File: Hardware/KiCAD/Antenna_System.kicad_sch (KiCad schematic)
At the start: 21 parts, among them IC4 SA630D_01,118, IC6 SA630D_01,118, J2 Conn_Coaxial_UHF

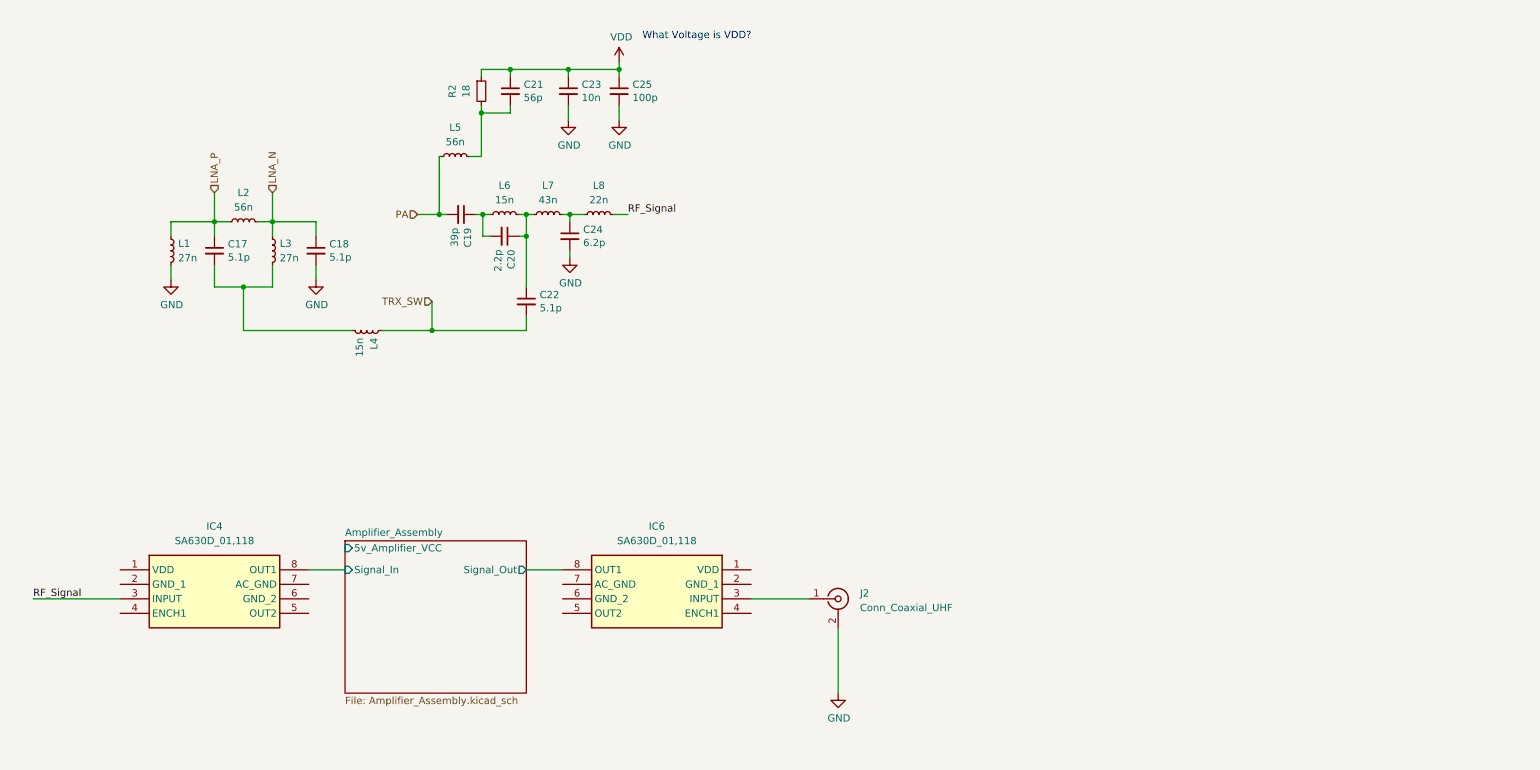
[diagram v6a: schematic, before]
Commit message: feat: subsystem exploration, begin placement, routing #11 #12 #4 many new project symbols
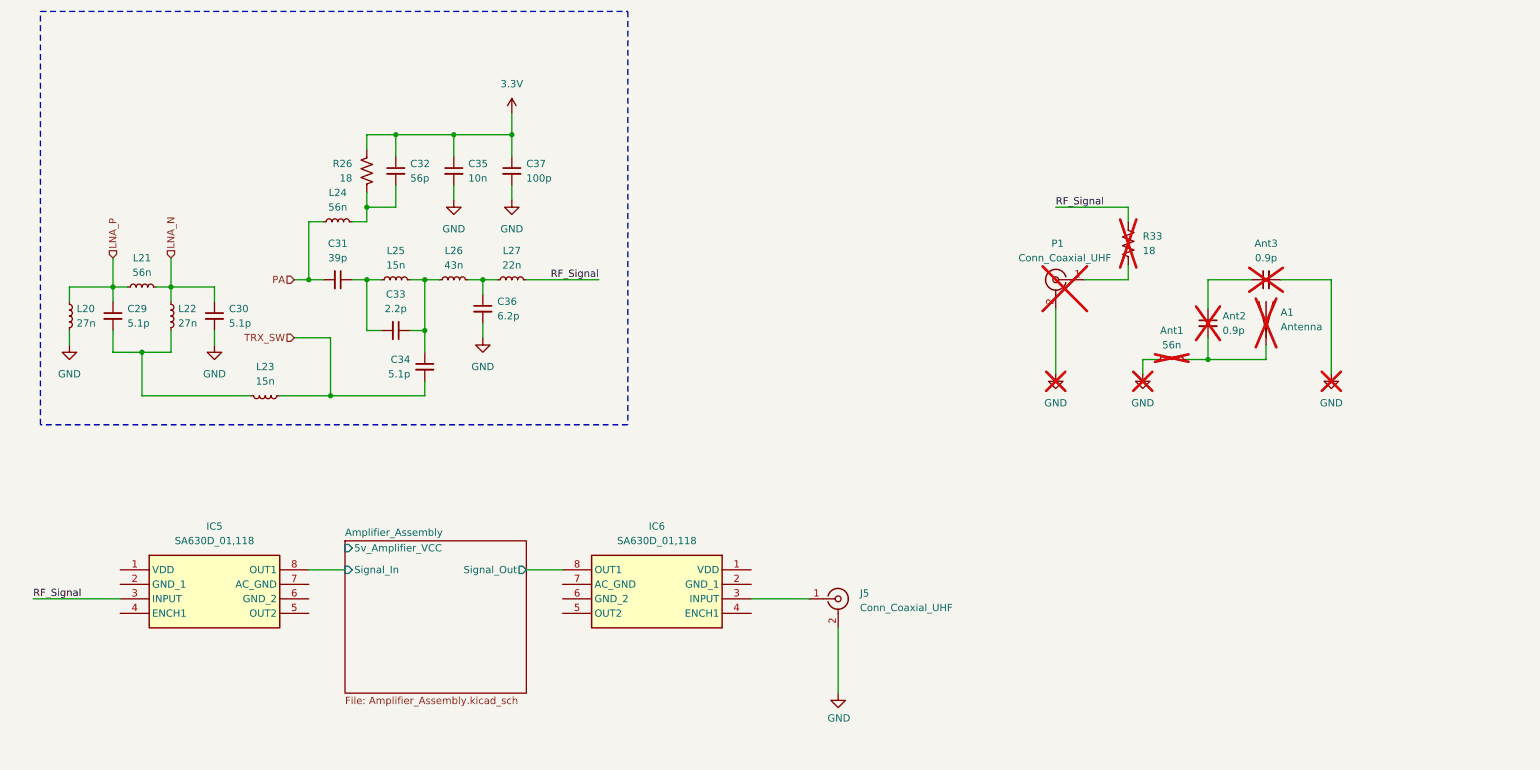
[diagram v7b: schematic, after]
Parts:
- removed C17, C18, C22: 5.1p, Capacitor_SMD:C_0402_1005Metric, symbol pkl_device:pkl_C_Small
- removed C19: 39p, Capacitor_SMD:C_0402_1005Metric, symbol pkl_device:pkl_C_Small
- removed C20: 2.2p, Capacitor_SMD:C_0402_1005Metric, symbol pkl_device:pkl_C_Small
- removed C21: 56p, Capacitor_SMD:C_0402_1005Metric, symbol pkl_device:pkl_C_Small
- removed C23: 10n, Capacitor_SMD:C_0402_1005Metric, symbol pkl_device:pkl_C_Small
- removed C24: 6.2p, Capacitor_SMD:C_0402_1005Metric, symbol pkl_device:pkl_C_Small
- removed C25: 100p, Capacitor_SMD:C_0402_1005Metric, symbol pkl_device:pkl_C_Small
- removed L1, L3: 27n, Inductor_SMD:L_0402_1005Metric, symbol Device:L_Small
- removed L2, L5: 56n, Inductor_SMD:L_0402_1005Metric, symbol Device:L_Small
- removed L4, L6: 15n, Inductor_SMD:L_0402_1005Metric, symbol Device:L_Small
- removed L7: 43n, Inductor_SMD:L_0402_1005Metric, symbol Device:L_Small
- removed L8: 22n, Inductor_SMD:L_0402_1005Metric, symbol Device:L_Small
- removed R2: 18, Resistor_SMD:R_0402_1005Metric, symbol pkl_device:pkl_R_Small
- added A1: Antenna, symbol Device:Antenna
- added Ant1, L21, L24: 56n, Inductor_SMD:L_0402_1005Metric, symbol Device:L_Small
- added Ant2, Ant3: 0.9p, Capacitor_SMD:C_0402_1005Metric, symbol Device:C_Small
- added C29, C30, C34: 5.1p, Capacitor_SMD:C_0402_1005Metric, symbol Device:C_Small
- added C31: 39p, Capacitor_SMD:C_0402_1005Metric, symbol Device:C_Small
- added C32: 56p, Capacitor_SMD:C_0402_1005Metric, symbol Device:C_Small
- added C33: 2.2p, Capacitor_SMD:C_0402_1005Metric, symbol Device:C_Small
- added C35: 10n, Capacitor_SMD:C_0402_1005Metric, symbol Device:C_Small
- added C36: 6.2p, Capacitor_SMD:C_0402_1005Metric, symbol Device:C_Small
- added C37: 100p, Capacitor_SMD:C_0402_1005Metric, symbol Device:C_Small
- added L20, L22: 27n, Inductor_SMD:L_0402_1005Metric, symbol Device:L_Small
- added L23, L25: 15n, Inductor_SMD:L_0402_1005Metric, symbol Device:L_Small
- added L26: 43n, Inductor_SMD:L_0402_1005Metric, symbol Device:L_Small
- added L27: 22n, Inductor_SMD:L_0402_1005Metric, symbol Device:L_Small
- added P1: Conn_Coaxial_UHF, Connector_Coaxial:SMA_Amphenol_901-143_Horizontal, symbol Connector:Conn_Coaxial
- added R26, R33: 18, Resistor_SMD:R_0402_1005Metric, symbol Device:R_US
- J5: renamed from J2; footprint Connector_Coaxial:SMA_Amphenol_901-143_Horizontal -> Connector_Coaxial:SMA_Molex_73251-1153_EdgeMount_Horizontal
- renumbered IC4 to IC5
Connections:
- net GND: now also Ant1.2, Ant3.2, C30.2, C35.2, C36.2, C37.2, L20.2, P1.2 (Ext)
- net LNA_N: now also C30.1, L21.2, L22.1
- net LNA_P: now also C29.1, L20.1, L21.1
- net PA: now also C31.2, L24.1
- net RF_Signal: now also L27.2, R33.2
- net TRX_SW: now also C34.2, L23.1
- new net: C31.1, C33.2, L25.1
- new net: C32.2, L24.2, R26.2
- new net: A1.1 (A), Ant1.1, Ant2.2
- new net: C29.2, L22.2, L23.2
- new net: P1.1 (In), R33.1
- new net: Ant2.1, Ant3.1
- new net: C36.1, L26.2, L27.1
- new net: C33.1, C34.1, L25.2, L26.1
- new net 3.3V: C32.1, C35.1, C37.1, R26.1
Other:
- note removed: "What Voltage is VDD?"
